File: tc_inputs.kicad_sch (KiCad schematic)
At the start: 2 parts, among them J1 Conn_01x02_Socket, J6 Conn_01x04_Socket

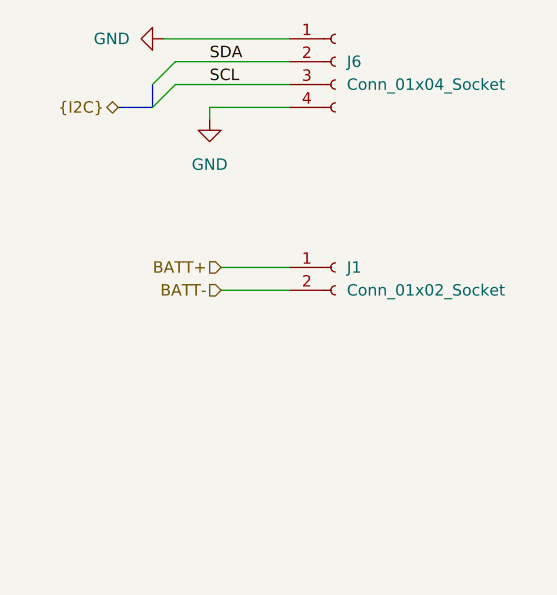
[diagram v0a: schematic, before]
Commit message: Fixing and cleaning up schematic
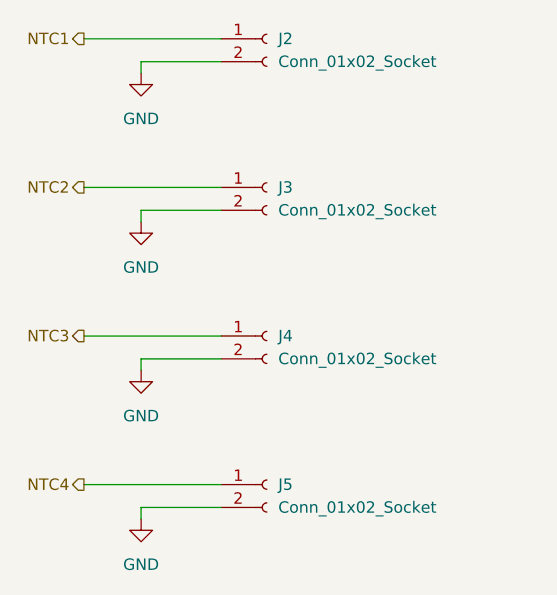
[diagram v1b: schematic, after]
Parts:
- removed J1: Conn_01x02_Socket, symbol Connector:Conn_01x02_Socket
- removed J6: Conn_01x04_Socket, symbol Connector:Conn_01x04_Socket
- added J2, J3, J4, J5: Conn_01x02_Socket, symbol Connector:Conn_01x02_Socket
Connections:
- net GND: now also J2.2 (Pin_2), J3.2 (Pin_2), J4.2 (Pin_2), J5.2 (Pin_2)
- new net NTC1: J2.1 (Pin_1)
- new net NTC2: J3.1 (Pin_1)
- new net NTC3: J4.1 (Pin_1)
- new net NTC4: J5.1 (Pin_1)

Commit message: Adding in diodes and fixing circuit
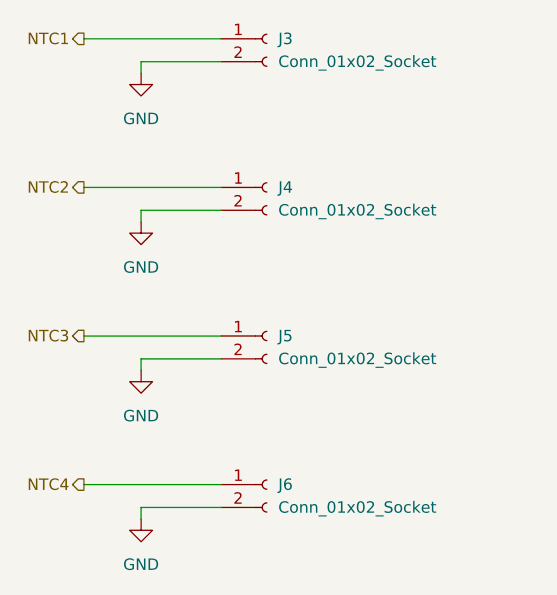
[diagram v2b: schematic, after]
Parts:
- renumbered J2 to J3, J3 to J4, J4 to J5, J5 to J6
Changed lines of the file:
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@@
 		(dnp no)
 		(fields_autoplaced yes)
-		(property "Reference" "J4"
+		(property "Reference" "J5"
 			(at 134.62 109.2199 0)
 			(effects
@@
 			(project "BMS"
 				(path "/124184ba-5d68-4d9f-8da6-acc6720ab30b/93f9b420-7cce-46a9-9201-666f07a18f85/959b991c-ec85-4b75-adc9-c8d386142e8b"
-					(reference "J4")
+					(reference "J5")
 					(unit 1)
 				)
@@
 		(dnp no)
 		(fields_autoplaced yes)
-		(property "Reference" "J2"
+		(property "Reference" "J3"
 			(at 134.62 76.1999 0)
 			(effects
@@
 			(project ""
 				(path "/124184ba-5d68-4d9f-8da6-acc6720ab30b/93f9b420-7cce-46a9-9201-666f07a18f85/959b991c-ec85-4b75-adc9-c8d386142e8b"
-					(reference "J2")
+					(reference "J3")
 					(unit 1)
 				)
@@
 		(dnp no)
 		(fields_autoplaced yes)
-		(property "Reference" "#PWR014"
+		(property "Reference" "#PWR03"
 			(at 119.38 86.36 0)
 			(effects
@@
 			(project ""
 				(path "/124184ba-5d68-4d9f-8da6-acc6720ab30b/93f9b420-7cce-46a9-9201-666f07a18f85/959b991c-ec85-4b75-adc9-c8d386142e8b"
-					(reference "#PWR014")
+					(reference "#PWR03")
 					(unit 1)
 				)
@@
 		(dnp no)
 		(fields_autoplaced yes)
-		(property "Reference" "#PWR019"
+		(property "Reference" "#PWR06"
 			(at 119.38 135.89 0)
 			(effects
@@
 			(project "BMS"
 				(path "/124184ba-5d68-4d9f-8da6-acc6720ab30b/93f9b420-7cce-46a9-9201-666f07a18f85/959b991c-ec85-4b75-adc9-c8d386142e8b"
-					(reference "#PWR019")
+					(reference "#PWR06")
 					(unit 1)
 				)
@@
 		(dnp no)
 		(fields_autoplaced yes)
-		(property "Reference" "#PWR018"
+		(property "Reference" "#PWR05"
 			(at 119.38 119.38 0)
 			(effects
@@
 			(project "BMS"
 				(path "/124184ba-5d68-4d9f-8da6-acc6720ab30b/93f9b420-7cce-46a9-9201-666f07a18f85/959b991c-ec85-4b75-adc9-c8d386142e8b"
-					(reference "#PWR018")
+					(reference "#PWR05")
 					(unit 1)
 				)
@@
 		(dnp no)
 		(fields_autoplaced yes)
-		(property "Reference" "J5"
+		(property "Reference" "J6"
 			(at 134.62 125.7299 0)
 			(effects
@@
 			(project "BMS"
 				(path "/124184ba-5d68-4d9f-8da6-acc6720ab30b/93f9b420-7cce-46a9-9201-666f07a18f85/959b991c-ec85-4b75-adc9-c8d386142e8b"
-					(reference "J5")
+					(reference "J6")
 					(unit 1)
 				)
@@
 		(dnp no)
 		(fields_autoplaced yes)
-		(property "Reference" "J3"
+		(property "Reference" "J4"
 			(at 134.62 92.7099 0)
 			(effects
@@
 			(project "BMS"
 				(path "/124184ba-5d68-4d9f-8da6-acc6720ab30b/93f9b420-7cce-46a9-9201-666f07a18f85/959b991c-ec85-4b75-adc9-c8d386142e8b"
-					(reference "J3")
+					(reference "J4")
 					(unit 1)
 				)
@@
 		(dnp no)
 		(fields_autoplaced yes)
-		(property "Reference" "#PWR017"
+		(property "Reference" "#PWR04"
 			(at 119.38 102.87 0)
 			(effects
@@
 			(project "BMS"
 				(path "/124184ba-5d68-4d9f-8da6-acc6720ab30b/93f9b420-7cce-46a9-9201-666f07a18f85/959b991c-ec85-4b75-adc9-c8d386142e8b"
-					(reference "#PWR017")
-					(unit 1)
-				)
+					(reference "#PWR04")
+					(unit 1)
+				)

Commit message: Updating schematic and adding in compnents to the PCB
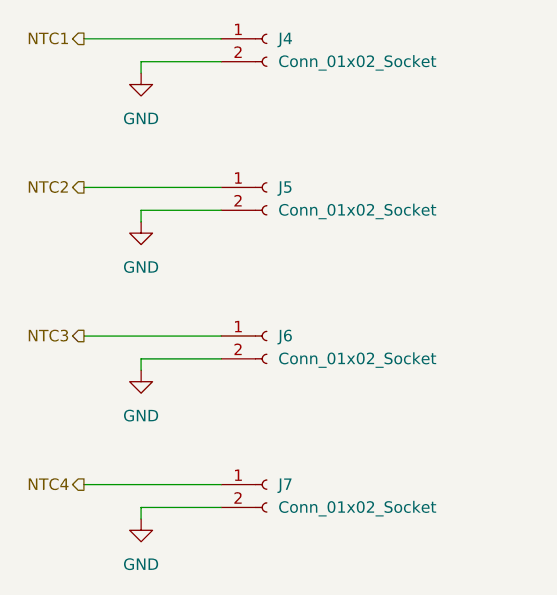
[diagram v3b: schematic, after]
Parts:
- renumbered J3 to J4, J4 to J5, J5 to J6, J6 to J7
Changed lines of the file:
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@@
 		(dnp no)
 		(fields_autoplaced yes)
-		(property "Reference" "J5"
+		(property "Reference" "J6"
 			(at 134.62 109.2199 0)
 			(effects
@@
 			(project "BMS"
 				(path "/124184ba-5d68-4d9f-8da6-acc6720ab30b/93f9b420-7cce-46a9-9201-666f07a18f85/959b991c-ec85-4b75-adc9-c8d386142e8b"
-					(reference "J5")
+					(reference "J6")
 					(unit 1)
 				)
@@
 		(dnp no)
 		(fields_autoplaced yes)
-		(property "Reference" "J3"
+		(property "Reference" "J4"
 			(at 134.62 76.1999 0)
 			(effects
@@
 			(project ""
 				(path "/124184ba-5d68-4d9f-8da6-acc6720ab30b/93f9b420-7cce-46a9-9201-666f07a18f85/959b991c-ec85-4b75-adc9-c8d386142e8b"
-					(reference "J3")
+					(reference "J4")
 					(unit 1)
 				)
@@
 		(dnp no)
 		(fields_autoplaced yes)
-		(property "Reference" "#PWR03"
+		(property "Reference" "#PWR05"
 			(at 119.38 86.36 0)
 			(effects
@@
 			(project ""
 				(path "/124184ba-5d68-4d9f-8da6-acc6720ab30b/93f9b420-7cce-46a9-9201-666f07a18f85/959b991c-ec85-4b75-adc9-c8d386142e8b"
-					(reference "#PWR03")
+					(reference "#PWR05")
 					(unit 1)
 				)
@@
 		(dnp no)
 		(fields_autoplaced yes)
-		(property "Reference" "#PWR06"
+		(property "Reference" "#PWR08"
 			(at 119.38 135.89 0)
 			(effects
@@
 			(project "BMS"
 				(path "/124184ba-5d68-4d9f-8da6-acc6720ab30b/93f9b420-7cce-46a9-9201-666f07a18f85/959b991c-ec85-4b75-adc9-c8d386142e8b"
-					(reference "#PWR06")
+					(reference "#PWR08")
 					(unit 1)
 				)
@@
 		(dnp no)
 		(fields_autoplaced yes)
-		(property "Reference" "#PWR05"
+		(property "Reference" "#PWR07"
 			(at 119.38 119.38 0)
 			(effects
@@
 			(project "BMS"
 				(path "/124184ba-5d68-4d9f-8da6-acc6720ab30b/93f9b420-7cce-46a9-9201-666f07a18f85/959b991c-ec85-4b75-adc9-c8d386142e8b"
-					(reference "#PWR05")
+					(reference "#PWR07")
 					(unit 1)
 				)
@@
 		(dnp no)
 		(fields_autoplaced yes)
-		(property "Reference" "J6"
+		(property "Reference" "J7"
 			(at 134.62 125.7299 0)
 			(effects
@@
 			(project "BMS"
 				(path "/124184ba-5d68-4d9f-8da6-acc6720ab30b/93f9b420-7cce-46a9-9201-666f07a18f85/959b991c-ec85-4b75-adc9-c8d386142e8b"
-					(reference "J6")
+					(reference "J7")
 					(unit 1)
 				)
@@
 		(dnp no)
 		(fields_autoplaced yes)
-		(property "Reference" "J4"
+		(property "Reference" "J5"
 			(at 134.62 92.7099 0)
 			(effects
@@
 			(project "BMS"
 				(path "/124184ba-5d68-4d9f-8da6-acc6720ab30b/93f9b420-7cce-46a9-9201-666f07a18f85/959b991c-ec85-4b75-adc9-c8d386142e8b"
-					(reference "J4")
+					(reference "J5")
 					(unit 1)
 				)
@@
 		(dnp no)
 		(fields_autoplaced yes)
-		(property "Reference" "#PWR04"
+		(property "Reference" "#PWR06"
 			(at 119.38 102.87 0)
 			(effects
@@
 			(project "BMS"
 				(path "/124184ba-5d68-4d9f-8da6-acc6720ab30b/93f9b420-7cce-46a9-9201-666f07a18f85/959b991c-ec85-4b75-adc9-c8d386142e8b"
-					(reference "#PWR04")
-					(unit 1)
-				)
+					(reference "#PWR06")
+					(unit 1)
+				)

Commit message: Layed on board. Still need to route
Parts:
- removed J4, J5, J6, J7: Conn_01x02_Socket, symbol Connector:Conn_01x02_Socket
- added J5, J6, J7, J8: Conn_01x02_Pin, symbol Connector:Conn_01x02_Pin
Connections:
- net GND: now also J5.2 (Pin_2), J6.2 (Pin_2), J7.2 (Pin_2), J8.2 (Pin_2)
- net NTC1: now also J5.1 (Pin_1)
- net NTC2: now also J6.1 (Pin_1)
- net NTC3: now also J7.1 (Pin_1)
- net NTC4: now also J8.1 (Pin_1)
